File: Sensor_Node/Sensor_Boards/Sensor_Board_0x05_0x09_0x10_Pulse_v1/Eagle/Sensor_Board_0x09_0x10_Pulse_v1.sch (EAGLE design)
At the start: 21 parts, among them J3 1x3 RA Female .1", J4 ARDUINO_ISP, J6 1x3 RA Female .1", U2 ATMEGA328P_TQFP, Y1 8MHZ

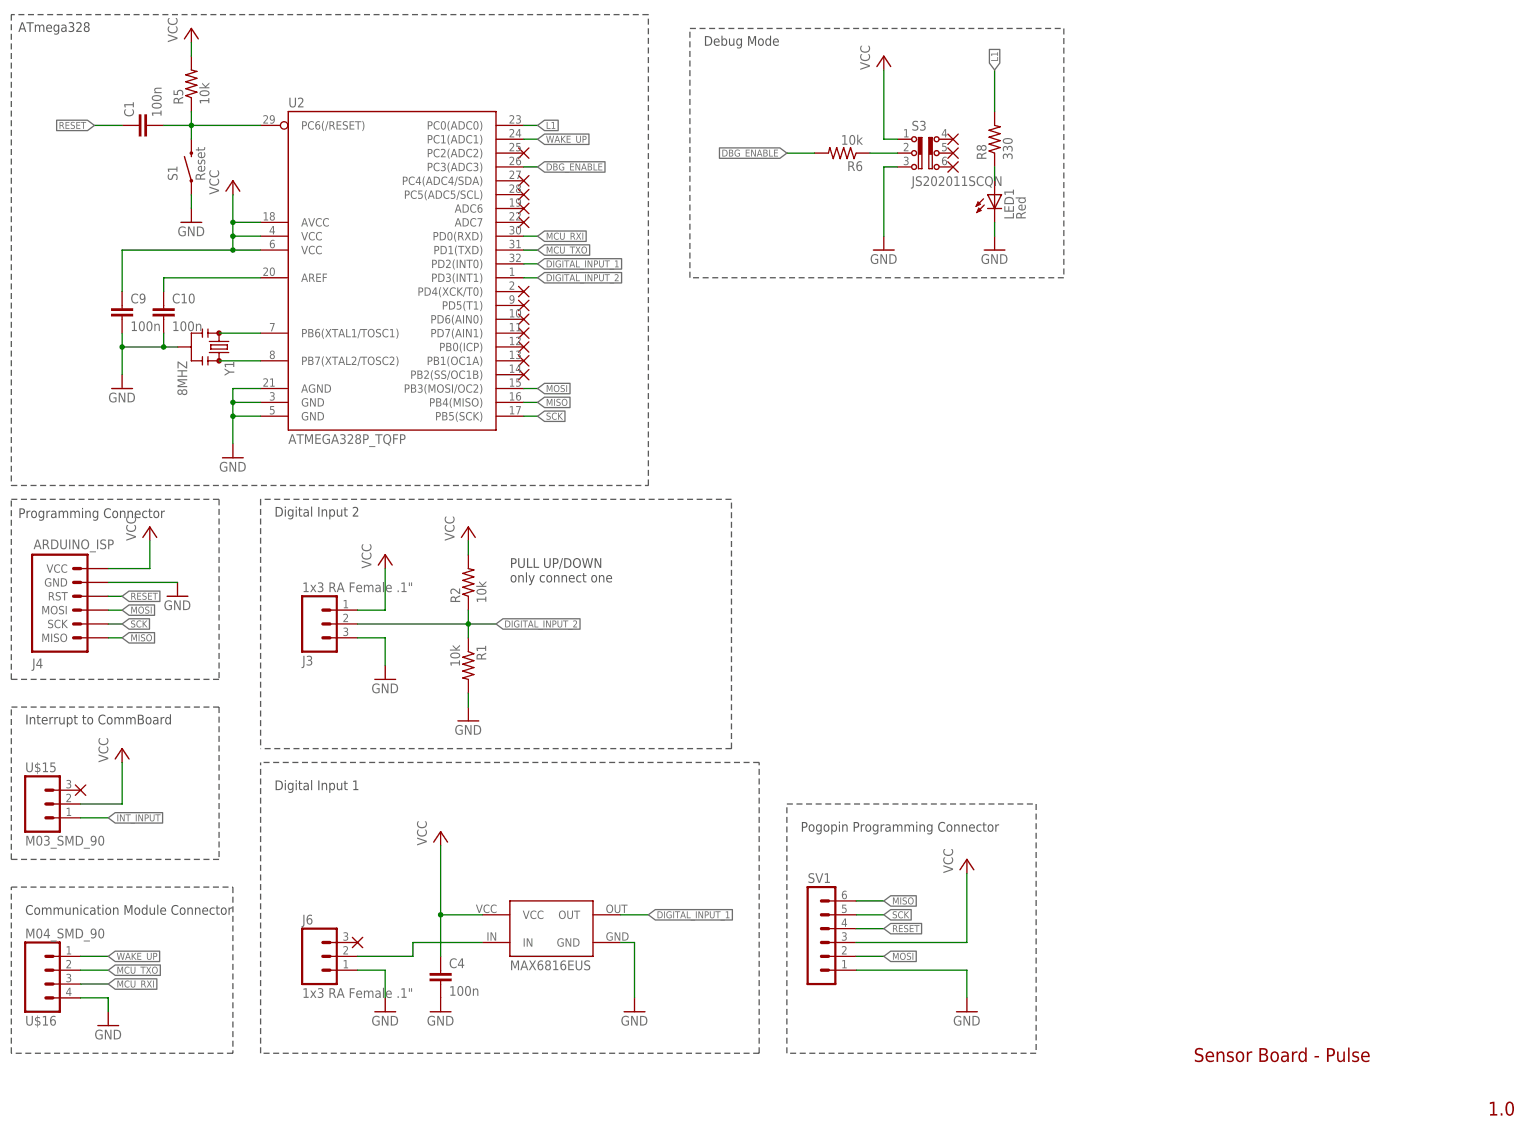
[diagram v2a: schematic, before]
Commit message: Changed some SensorBoards
SHT31
- new routing

PULSE
- pogopin programmer now over FTDI
- interrupt to comboard now comes from atmega

TSL2561
- pogopin programmer now over FTDI

PROTOYPING
- changed title of schematic
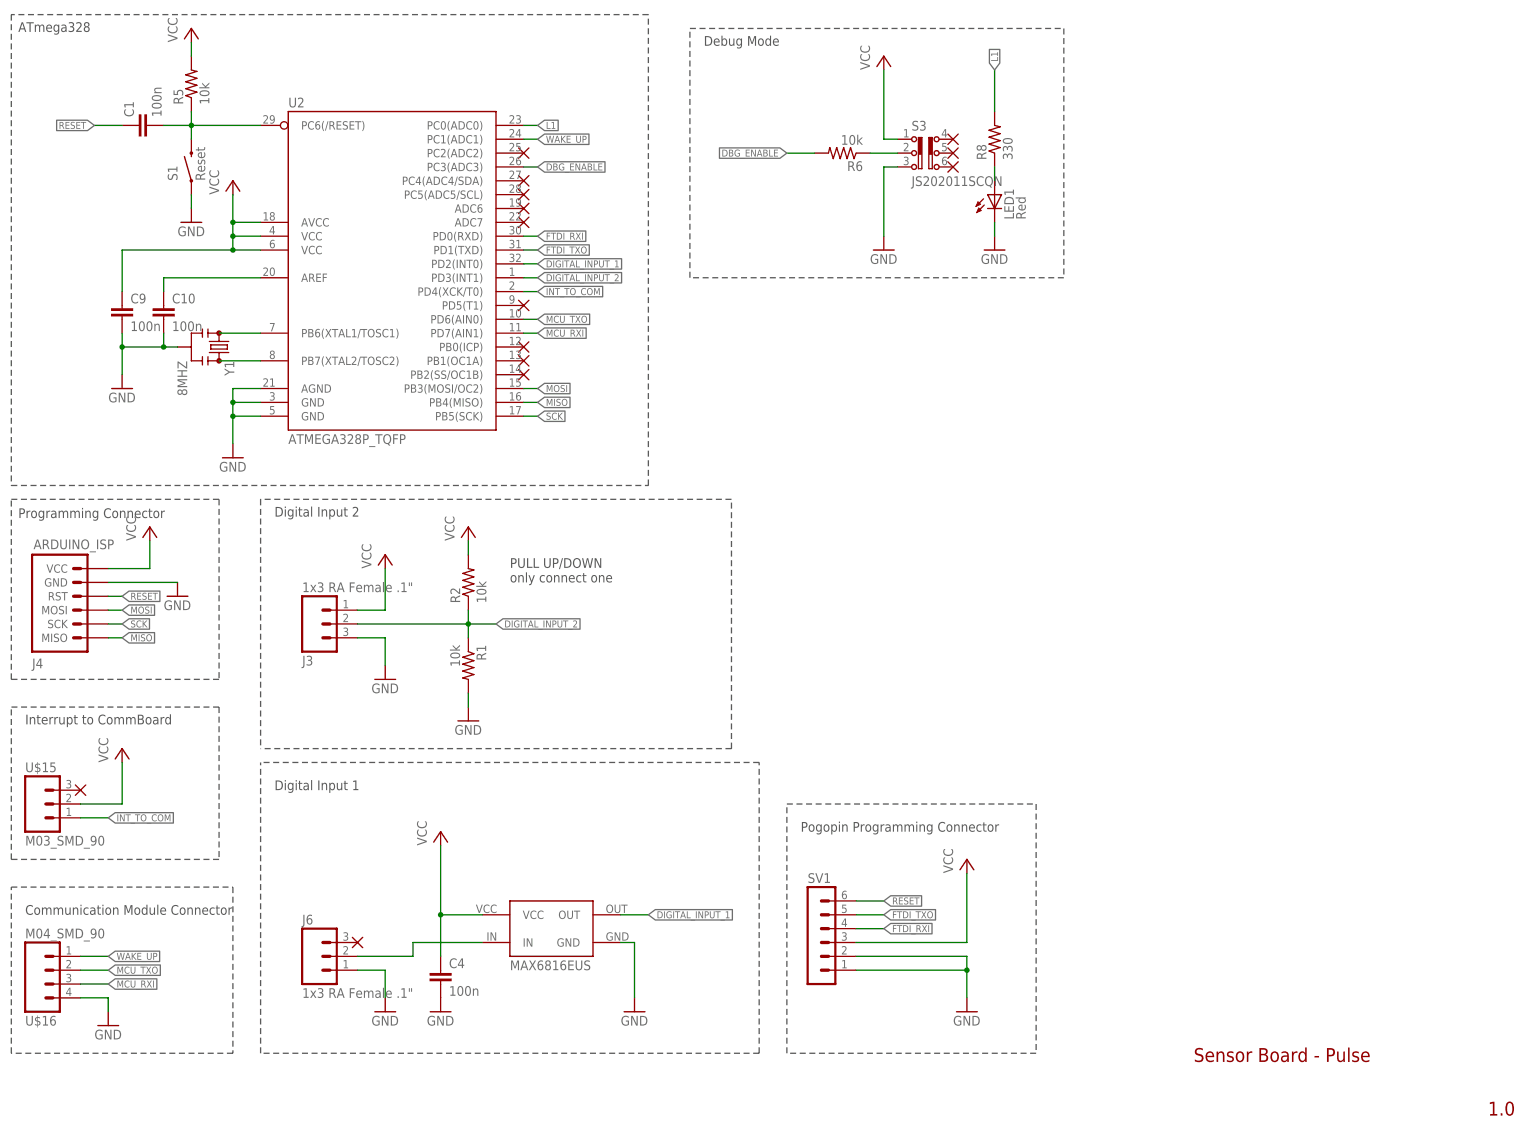
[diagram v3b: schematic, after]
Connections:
- removed net INT_INPUT: U$15.1
- new net FTDI_RXI: SV1.4, U2.PD0(RXD)
- new net FTDI_TXO: SV1.5, U2.PD1(TXD)
- new net INT_TO_COM: U$15.1, U2.PD4(XCK/T0)
- net GND: now also SV1.2
- net MCU_RXI: now also U2.PD7(AIN1); no longer U2.PD0(RXD)
- net MCU_TXO: now also U2.PD6(AIN0); no longer U2.PD1(TXD)
- net MISO: no longer SV1.6
- net MOSI: no longer SV1.2
- net RESET: now also SV1.6; no longer SV1.4
- net SCK: no longer SV1.5
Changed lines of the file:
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@@
 <part name="U$4" library="myownthings" deviceset="N/C" device=""/>
 <part name="U$5" library="myownthings" deviceset="N/C" device=""/>
-<part name="U$6" library="myownthings" deviceset="N/C" device=""/>
 <part name="U$7" library="myownthings" deviceset="N/C" device=""/>
-<part name="U$8" library="myownthings" deviceset="N/C" device=""/>
 <part name="U$9" library="myownthings" deviceset="N/C" device=""/>
-<part name="U$10" library="myownthings" deviceset="N/C" device=""/>
 <part name="U$11" library="myownthings" deviceset="N/C" device=""/>
 <part name="U$12" library="myownthings" deviceset="N/C" device=""/>
@@
 <instance part="U$4" gate="G$1" x="101.6" y="167.64"/>
 <instance part="U$5" gate="G$1" x="101.6" y="165.1"/>
-<instance part="U$6" gate="G$1" x="101.6" y="152.4"/>
 <instance part="U$7" gate="G$1" x="101.6" y="149.86"/>
-<instance part="U$8" gate="G$1" x="101.6" y="147.32"/>
 <instance part="U$9" gate="G$1" x="101.6" y="142.24"/>
-<instance part="U$10" gate="G$1" x="101.6" y="144.78"/>
 <instance part="U$11" gate="G$1" x="101.6" y="139.7"/>
 <instance part="U$12" gate="G$1" x="101.6" y="137.16"/>
@@
 <pinref part="SV1" gate="1" pin="1"/>
 <wire x1="182.88" y1="27.94" x2="162.56" y2="27.94" width="0.1524" layer="91"/>
+<pinref part="SV1" gate="1" pin="2"/>
+<wire x1="162.56" y1="30.48" x2="182.88" y2="30.48" width="0.1524" layer="91"/>
+<wire x1="182.88" y1="30.48" x2="182.88" y2="27.94" width="0.1524" layer="91"/>
+<junction x="182.88" y="27.94"/>
 </segment>
 </net>
@@
 </segment>
 <segment>
-<pinref part="SV1" gate="1" pin="4"/>
-<wire x1="162.56" y1="35.56" x2="167.64" y2="35.56" width="0.1524" layer="91"/>
-<label x="167.64" y="35.56" size="1.27" layer="95" xref="yes"/>
+<pinref part="SV1" gate="1" pin="6"/>
+<wire x1="162.56" y1="40.64" x2="167.64" y2="40.64" width="0.1524" layer="91"/>
+<label x="167.64" y="40.64" size="1.27" layer="95" xref="yes"/>
 </segment>
 </net>
@@
 <pinref part="U2" gate="U$1" pin="PB5(SCK)"/>
 </segment>
-<segment>
-<pinref part="SV1" gate="1" pin="5"/>
-<wire x1="162.56" y1="38.1" x2="167.64" y2="38.1" width="0.1524" layer="91"/>
-<label x="167.64" y="38.1" size="1.27" layer="95" xref="yes"/>
-</segment>
 </net>
 <net name="MISO" class="0">
@@
 <pinref part="U2" gate="U$1" pin="PB4(MISO)"/>
 </segment>
-<segment>
-<pinref part="SV1" gate="1" pin="6"/>
-<wire x1="162.56" y1="40.64" x2="167.64" y2="40.64" width="0.1524" layer="91"/>
-<label x="167.64" y="40.64" size="1.27" layer="95" xref="yes"/>
-</segment>
 </net>
 <net name="MOSI" class="0">
@@
 <pinref part="U2" gate="U$1" pin="PB3(MOSI/OC2)"/>
 </segment>
-<segment>
-<pinref part="SV1" gate="1" pin="2"/>
-<wire x1="162.56" y1="30.48" x2="167.64" y2="30.48" width="0.1524" layer="91"/>
-<label x="167.64" y="30.48" size="1.27" layer="95" xref="yes"/>
-</segment>
 </net>
 <net name="MCU_TXO" class="0">
-<segment>
-<wire x1="101.6" y1="160.02" x2="104.14" y2="160.02" width="0.1524" layer="91"/>
-<label x="104.14" y="160.02" size="1.27" layer="95" xref="yes"/>
-<pinref part="U2" gate="U$1" pin="PD1(TXD)"/>
-</segment>
 <segment>
 <wire x1="20.32" y1="27.94" x2="25.4" y2="27.94" width="0.1524" layer="91"/>
@@
 <pinref part="U$16" gate="G$1" pin="2"/>
 </segment>
+<segment>
+<pinref part="U2" gate="U$1" pin="PD6(AIN0)"/>
+<wire x1="101.6" y1="147.32" x2="104.14" y2="147.32" width="0.1524" layer="91"/>
+<label x="104.14" y="147.32" size="1.27" layer="95" xref="yes"/>
+</segment>
 </net>
 <net name="L1" class="0">
@@
 <net name="MCU_RXI" class="0">
 <segment>
-<wire x1="101.6" y1="162.56" x2="104.14" y2="162.56" width="0.1524" layer="91"/>
-<label x="104.14" y="162.56" size="1.27" layer="95" xref="yes"/>
-<pinref part="U2" gate="U$1" pin="PD0(RXD)"/>
-</segment>
-<segment>
 <wire x1="20.32" y1="25.4" x2="25.4" y2="25.4" width="0.1524" layer="91"/>
 <label x="25.4" y="25.4" size="1.27" layer="95" xref="yes"/>
 <pinref part="U$16" gate="G$1" pin="3"/>
+</segment>
+<segment>
+<pinref part="U2" gate="U$1" pin="PD7(AIN1)"/>
+<wire x1="101.6" y1="144.78" x2="104.14" y2="144.78" width="0.1524" layer="91"/>
+<label x="104.14" y="144.78" size="1.27" layer="95" xref="yes"/>
 </segment>
 </net>
@@
 </segment>
 </net>
-<net name="INT_INPUT" class="0">
+<net name="INT_TO_COM" class="0">
 <segment>
 <pinref part="U$15" gate="G$1" pin="1"/>
 <wire x1="20.32" y1="55.88" x2="25.4" y2="55.88" width="0.1524" layer="91"/>
 <label x="25.4" y="55.88" size="1.27" layer="95" xref="yes"/>
+</segment>
+<segment>
+<pinref part="U2" gate="U$1" pin="PD4(XCK/T0)"/>
+<wire x1="101.6" y1="152.4" x2="104.14" y2="152.4" width="0.1524" layer="91"/>
+<label x="104.14" y="152.4" size="1.27" layer="95" xref="yes"/>
 </segment>
 </net>
@@
 </segment>
 </net>
+<net name="FTDI_RXI" class="0">
+<segment>
+<wire x1="101.6" y1="162.56" x2="104.14" y2="162.56" width="0.1524" layer="91"/>
+<label x="104.14" y="162.56" size="1.27" layer="95" xref="yes"/>
+<pinref part="U2" gate="U$1" pin="PD0(RXD)"/>
+</segment>
+<segment>
+<pinref part="SV1" gate="1" pin="4"/>
+<wire x1="162.56" y1="35.56" x2="167.64" y2="35.56" width="0.1524" layer="91"/>
+<label x="167.64" y="35.56" size="1.27" layer="95" xref="yes"/>
+</segment>
+</net>
+<net name="FTDI_TXO" class="0">
+<segment>
+<wire x1="101.6" y1="160.02" x2="104.14" y2="160.02" width="0.1524" layer="91"/>
+<label x="104.14" y="160.02" size="1.27" layer="95" xref="yes"/>
+<pinref part="U2" gate="U$1" pin="PD1(TXD)"/>
+</segment>
+<segment>
+<pinref part="SV1" gate="1" pin="5"/>
+<wire x1="162.56" y1="38.1" x2="167.64" y2="38.1" width="0.1524" layer="91"/>
+<label x="167.64" y="38.1" size="1.27" layer="95" xref="yes"/>
+</segment>
+</net>
